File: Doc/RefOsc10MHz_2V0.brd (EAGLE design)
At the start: 88.9 x 69.8 mm, 74 parts, among them CON11 MCX-J-P-X-RA-SM1, CON2 HEADER-2X5SMD, CON3 1-227161-0, CON4 AVR-ISP-10SMD, CON5 AVR-JTAG-10SMD, IC1 ATmega328-P, IC11 712-RXM-GNSS-TM-B, IC2 LC4032V_XXT44, IC202 CFPT-126, IC3 74HCT221D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

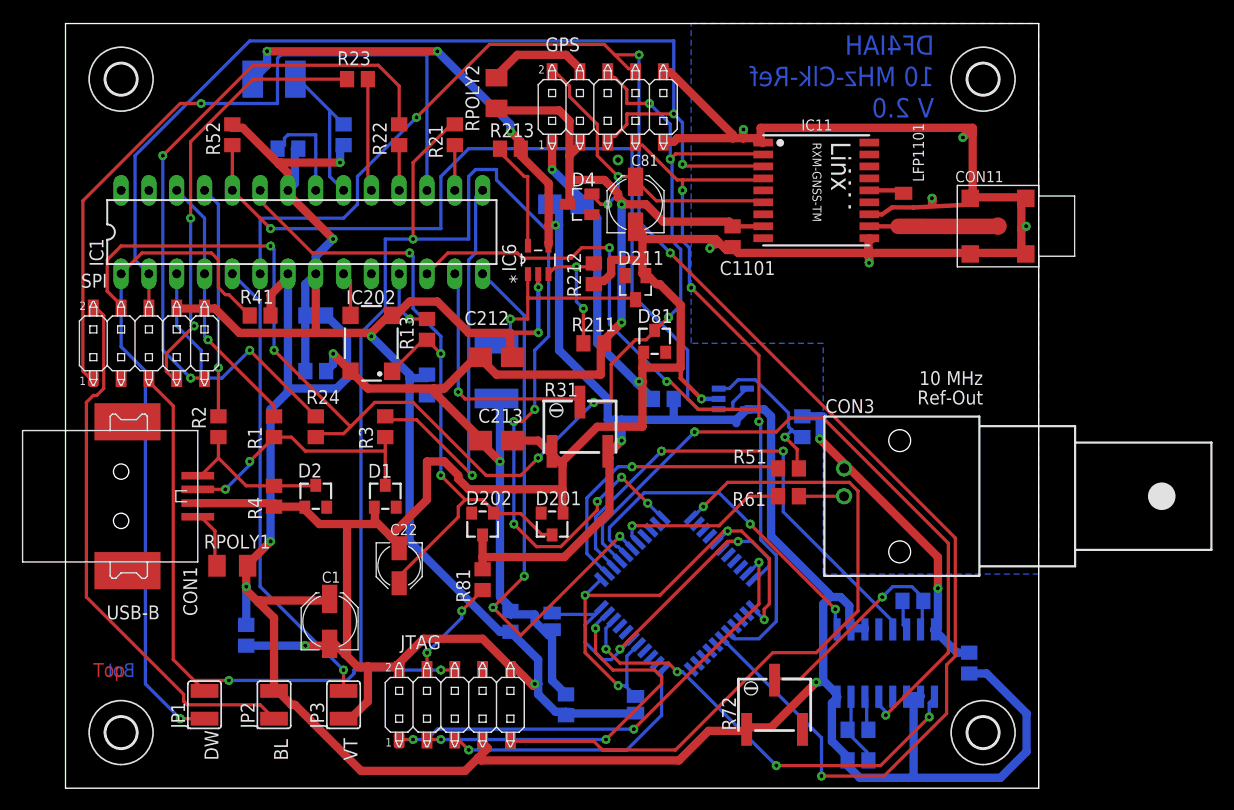
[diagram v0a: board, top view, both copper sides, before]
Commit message: avr_DF4IAH_Bootloader - Doc - Eagle: I2C header added
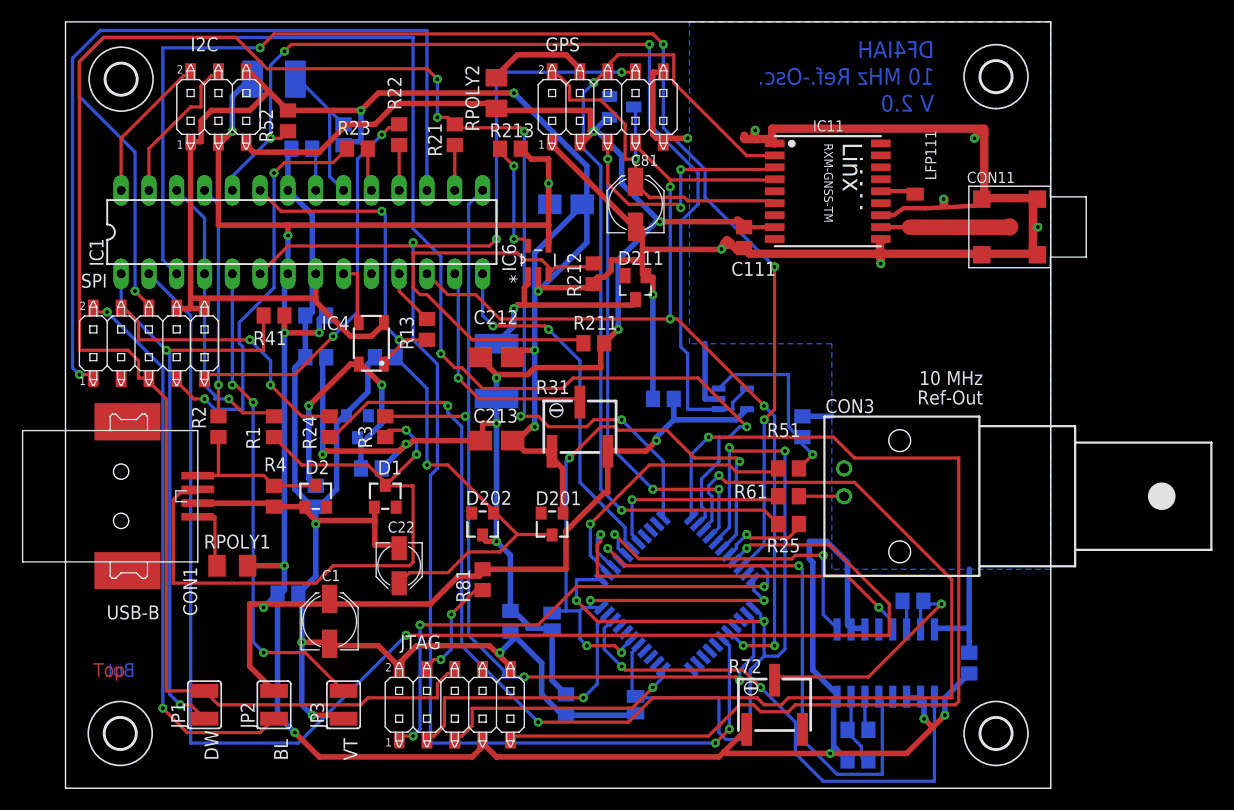
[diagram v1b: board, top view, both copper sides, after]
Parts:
- removed C1101: 100n, df4iah:C0805
- removed D4: BAS70-04, diode:SOT23
- removed D81: BZX84-C3V6, diode:TO236
- removed IC202: CFPT-126, df4iah:SM77H
- removed LFP1101: WE-CBF_300R, df4iah:L3216C
- added C111: 100n, df4iah:C0805
- added C221: 100n, rcl:C0805
- added CON6: HEADER-2X3SMD, df4iah:2X03SMD
- added D221: BZX84-C3V0, diode:TO236
- added D82: CRS08, diode:SOT23
- added IC4: CFPT-141, df4iah:CFPT-141
- added LFP111: WE-CBF_300R, df4iah:L3216C
- added R221: 56, rcl:R0805
- added R25: 2.7k, rcl:R0805
- R61: value 47 -> 51
- moved R23 6.35 mm to (26.7, 58.4)
- moved C2 5.39 mm to (20.3, 17.8), turned to 180 degrees
- moved R52 5.24 mm to (20.3, 61.0)
- moved C21 4.58 mm to (29.2, 39.4), turned to 0 degrees
- moved C32 1.27 mm to (21.6, 58.4), turned to 0 degrees
- moved R24 1.27 mm to (24.1, 33.0), turned to 90 degrees
- moved R41 1.27 mm to (19.1, 43.2)
- moved C203 1.27 mm to (22.9, 39.4)
- moved U$1 1.20 mm to (85.0, 65.0)
- moved U$2 1.18 mm to (85.0, 5.00)
- moved CON11 1.06 mm to (86.2, 51.3)
- moved IC11 1.06 mm to (69.6, 54.5)
- moved U$3 0.11 mm to (5.00, 5.00), turned to 180 degrees
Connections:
- removed net TXD: IC1.3, R24.1
- new net +3V0: C221.1, D221.C, IC4.4, R221.2
- new net CPLD_GPS_NMEA_TX: IC2.7, R25.2
- new net CPLD_ISP_RXD: IC2.3, R24.1
- new net ISP_RXD: CON4.4, R24.2
- new net ISP_TXD: CON4.6, IC2.2
- new net MCU_RXD: IC1.2, IC2.8
- new net MCU_TXD: IC1.3, IC2.9
- new net N$1: CON6.2, IC1.28
- new net N$3: CON6.4, IC1.27
- net +3V3: now also C111.1, CON6.5, D202.C, D82.1, R221.1; no longer C1101.1, D4.3, IC202.4
- net 14: now also LFP111.1; no longer LFP1101.1
- net GND: now also C111.2, C221.2, CON6.1, CON6.6, D221.A, IC4.2; no longer C1101.2, D81.A, IC202.2
- net GPS_HF: now also LFP111.2; no longer LFP1101.2
- net GPS_NMEA_RX: now also IC2.4; no longer CON4.6, IC1.2
- net GPS_NMEA_TX: now also R25.1; no longer CON4.4, D81.C, R24.2
- net GPS_VBACKUP: now also D82.3; no longer D4.2
- net N_ADC_PULL: now also IC4.1; no longer IC202.1
- net N_USB_DISC: now also IC2.13
- net TOSC1: now also IC4.3; no longer IC202.3
- net VCC: now also CON6.3; no longer D202.C
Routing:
- net MCU_RXD: track 0.00 -> 132.2 mm, vias 0 -> 2
- net ISP_TXD: track 0.00 -> 129.9 mm, vias 0 -> 3
- net CPLD_ISP_RXD: track 0.00 -> 125.8 mm, vias 0 -> 3
- net MCU_TXD: track 0.00 -> 121.1 mm, vias 0 -> 4
- net N_USB_DISC: track 37.0 -> 82.7 mm, vias 1 -> 3
- net GND_SJ1: track 47.0 -> 89.0 mm
- net GPS_NMEA_TX: track 120.1 -> 79.3 mm, vias 7 -> 2
- net USB_D_MIN: track 24.2 -> 63.7 mm
- net VCC_3V3_SJ2: track 37.0 -> 73.1 mm, vias 2 -> 6
- net +3V3: track 124.1 -> 156.9 mm, vias 4 -> 8
- net JTAG_TDI: track 65.3 -> 96.9 mm
- net GPS_NMEA_RX: track 94.7 -> 66.2 mm, vias 2 -> 5
- net FB: track 12.1 -> 38.9 mm, vias 2 -> 0
- net +3V0: track 0.00 -> 26.4 mm, vias 0 -> 2
- net ISP_RXD: track 0.00 -> 25.4 mm, vias 0 -> 2
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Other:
- board size 88.9 x 69.8 mm -> 90 x 70 mm
- board text added: "DF4IAH 10 MHz Ref.-Osc. V 2.0"
- board text added: "I2C"
- board text removed: "DF4IAH 10 MHz-Clk-Ref V 2.0"

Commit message: avr_DF4IAH_Bootloader - Doc - Eagle: USB-B and BNC connectors changed
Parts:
- CON1: value (none) -> TYCO-AMP_USBUSB-B_SMT; device con-usb-3:USB-B-SMT -> df4iah:TYCO-AMP_USB-B_SMT
- CON3: value 1-227161-0 -> SD-73100-0105; device con-coax:AMP_227161 -> df4iah:MOLEX_BNC-JACK-50R_SD-73100-0105
- moved CON3 13.8 mm to (90.0, 26.6), turned to 180 degrees
- moved RPOLY1 5.68 mm to (12.7, 15.2)
- moved CON1 3.81 mm to (8.89, 26.7), turned to 180 degrees
- moved R2 1.80 mm to (15.2, 34.3), turned to 180 degrees
- turned JP1 to 270 degrees
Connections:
- net GND: now also CON1.4, CON3.3; no longer CON1.GND
- net USB_D_MIN: now also CON1.2; no longer CON1.D-
- net USB_D_PLS: now also CON1.3; no longer CON1.D+
- net USB_PWR: now also CON1.1; no longer CON1.VUSB
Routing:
- net ISP_SCK: track 38.0 -> 53.9 mm
- net USB_D_MIN: track 63.7 -> 52.5 mm
- net MCU_RXD: track 132.2 -> 138.9 mm
- net N$42: track 4.13 -> 10.7 mm, vias 0 -> 1
- net JTAG_SRST: track 186.8 -> 192.5 mm
- net USB_PWR: track 6.21 -> 11.3 mm
- net RESET: track 56.4 -> 53.3 mm
- net GND: track 453.0 -> 449.9 mm
- net N_USB_DPLS: track 21.2 -> 22.5 mm
- net GPS_HF: track 11.1 -> 12.1 mm
- net N_USB_DMNS: track 26.6 -> 27.2 mm
- net VCC: track 297.1 -> 296.4 mm, vias 12 -> 11
- net USB_D_PLS: track 14.7 -> 14.1 mm, vias 0 -> 2
- net INT1: track 44.7 -> 44.6 mm, vias 3 -> 1

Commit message: avr_DF4IAH_Bootloader - Doc - Eagle: ISP-Connector changed from old 10 to new 6 pin variant
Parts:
- removed R24: 2.7k, rcl:R0805
- CON4: value AVR-ISP-10SMD -> AVR-ISP-6SMD; device atmel-1:2X5SMD -> atmel-1:2X3SMD
- moved CON4 2.54 mm to (5.08, 40.6)
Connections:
- removed net CPLD_ISP_RXD: IC2.3, R24.1
- removed net ISP_RXD: CON4.4, R24.2
- removed net ISP_TXD: CON4.6, IC2.2
- net GND: now also CON4.6; no longer CON4.10, CON4.8
- net ISP_MISO: now also CON4.1; no longer CON4.9
- net ISP_MOSI: now also CON4.4; no longer CON4.1
- net ISP_SCK: now also CON4.3; no longer CON4.7
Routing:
- net ISP_TXD: track 129.9 -> 0.00 mm, vias 3 -> 0
- net CPLD_ISP_RXD: track 125.8 -> 0.00 mm, vias 3 -> 0
- net MCU_RXD: track 138.9 -> 81.0 mm
- net JTAG_SRST: track 192.5 -> 148.0 mm
- net ISP_RXD: track 25.4 -> 0.00 mm, vias 2 -> 0
- net ISP_MISO: track 35.8 -> 47.3 mm
- net ISP_SCK: track 53.9 -> 45.4 mm
- net ISP_MOSI: track 78.7 -> 72.0 mm
- net RESET: track 53.3 -> 58.4 mm, vias 2 -> 1
- net ISP_VTARGET: track 51.6 -> 55.3 mm, vias 2 -> 0
- net N_USB_DPLS: track 22.5 -> 21.2 mm
- net N_USB_DMNS: track 27.2 -> 26.3 mm
- net GND: track 449.9 -> 450.6 mm

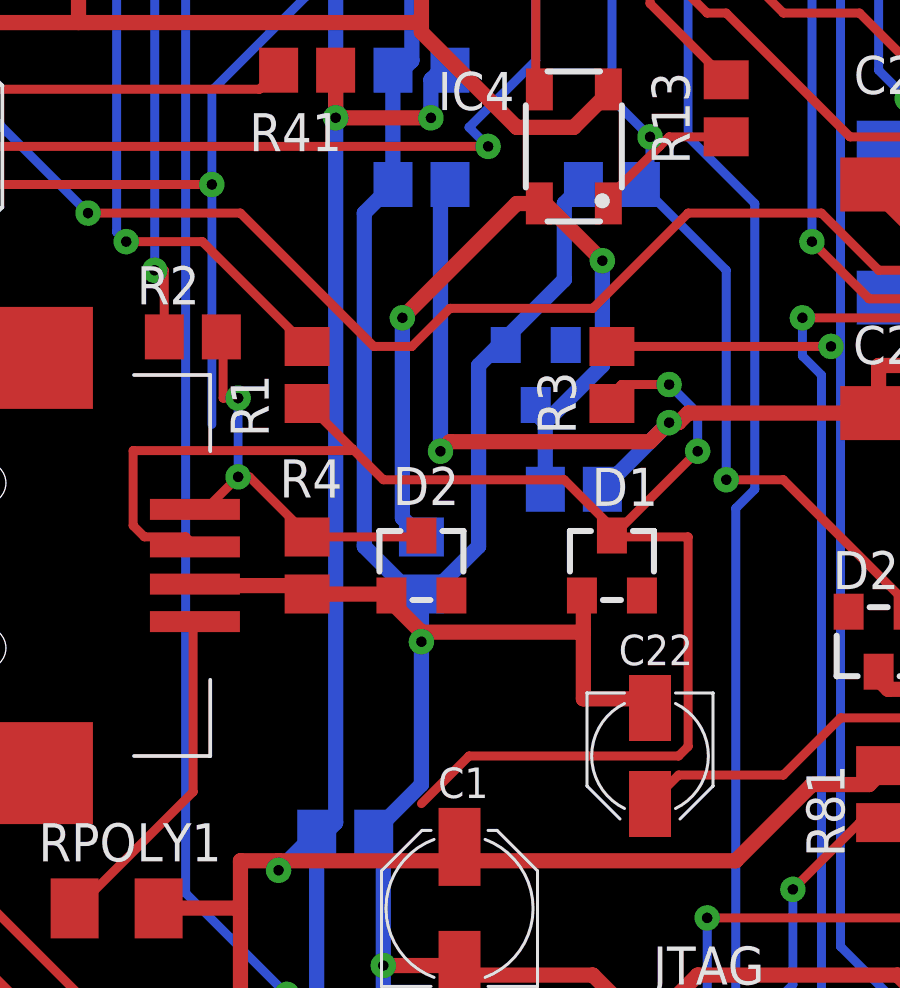
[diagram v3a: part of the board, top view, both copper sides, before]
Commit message: avr_DF4IAH_Bootloader - Doc - Eagle: V2.0.1 manufactured by PCB-Pool - corrections needed
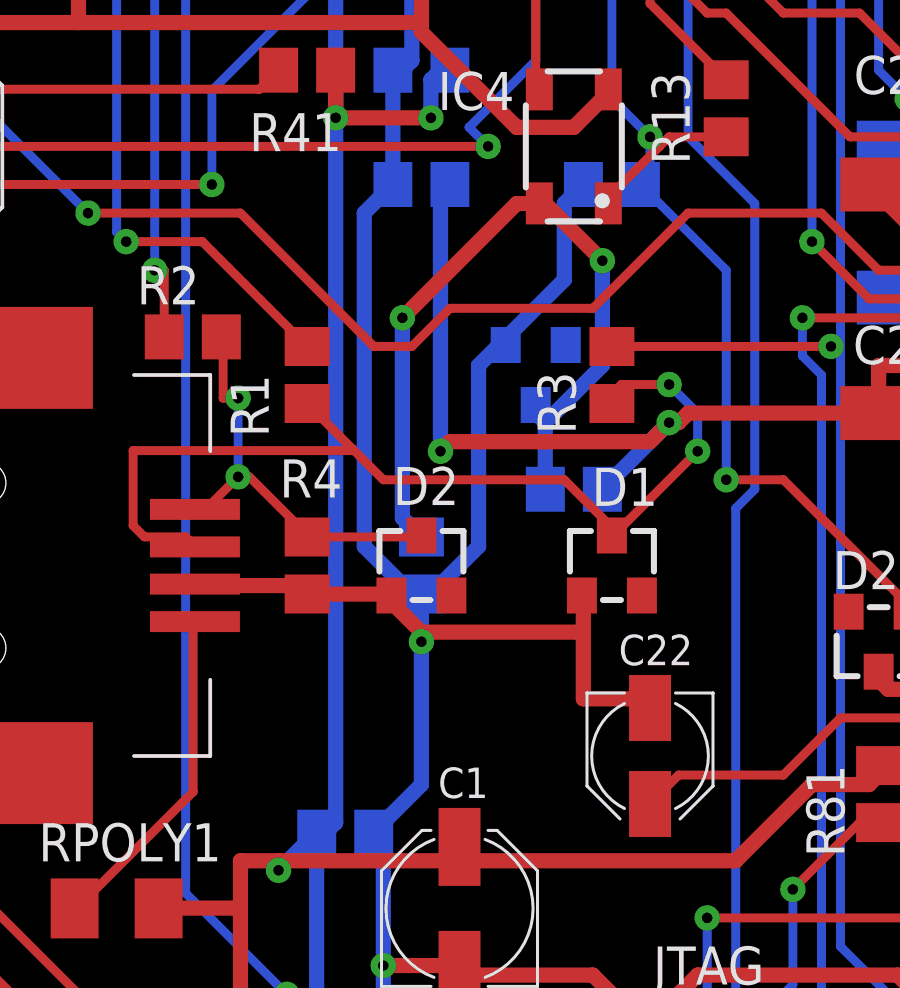
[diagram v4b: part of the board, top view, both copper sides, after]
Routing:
- net USB_D_MIN: track 52.5 -> 33.2 mm
- net ISP_SCK: track 45.4 -> 37.4 mm
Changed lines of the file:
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@@
 <wire x1="29.21" y1="32.385" x2="29.21" y2="32.07" width="0.3" layer="1"/>
 <wire x1="29.21" y1="27.94" x2="29.21" y2="27.67" width="0.3" layer="1"/>
-<wire x1="24.4475" y1="20.32" x2="22.86" y2="18.7325" width="0.3" layer="1"/>
-<wire x1="31.4325" y1="20.32" x2="24.4475" y2="20.32" width="0.3" layer="1"/>
-<wire x1="31.75" y1="20.6375" x2="31.4325" y2="20.32" width="0.3" layer="1"/>
-<wire x1="31.75" y1="27.6225" x2="31.75" y2="20.6375" width="0.3" layer="1"/>
-<wire x1="29.21" y1="27.6225" x2="31.75" y2="27.6225" width="0.3" layer="1"/>
-<wire x1="29.21" y1="27.6225" x2="29.21" y2="27.67" width="0.3" layer="1"/>
 <via x="31.115" y="32.7025" extent="1-16" drill="0.35"/>
 <via x="32.0675" y="30.48" extent="1-16" drill="0.35"/>
@@
 <via x="19.05" y="56.1975" extent="1-16" drill="0.35"/>
 <wire x1="15.875" y1="42.5" x2="15.875" y2="39.37" width="0.3" layer="16"/>
-<wire x1="15.875" y1="39.37" x2="15.875" y2="31.375" width="0.3" layer="16"/>
 <wire x1="19" y1="45.625" x2="15.875" y2="42.5" width="0.3" layer="16"/>
 <wire x1="19" y1="45.625" x2="19.05" y2="45.72" width="0.3" layer="16"/>
